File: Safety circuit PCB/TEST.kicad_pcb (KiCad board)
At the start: 2 copper layers, 101.5 x 54.2 mm, 36 parts, among them J1 430450801, J2 430450801, Q1 2N7002K, Q2 2N7002K, Q3 2N7002K, Q4 2N7002K, Q5 2N7002K, Q6 2N7002K, Q7 2N7002K

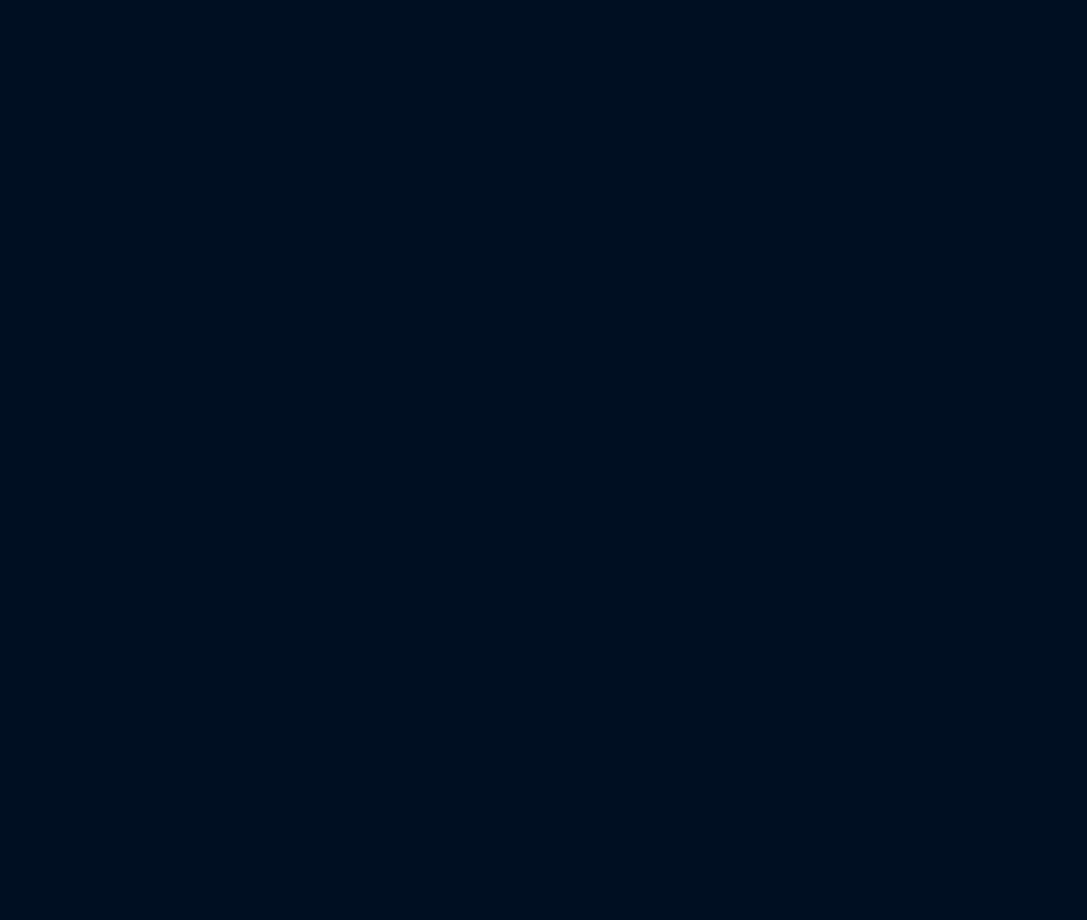
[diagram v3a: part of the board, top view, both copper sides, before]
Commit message: Add Sammy connector footprint to Safety Circuit PCB
The PCB layout still needs to be redone once again to actually fit the connector. It seems like it will have to be extended around 0.8 inches. at a minimum.
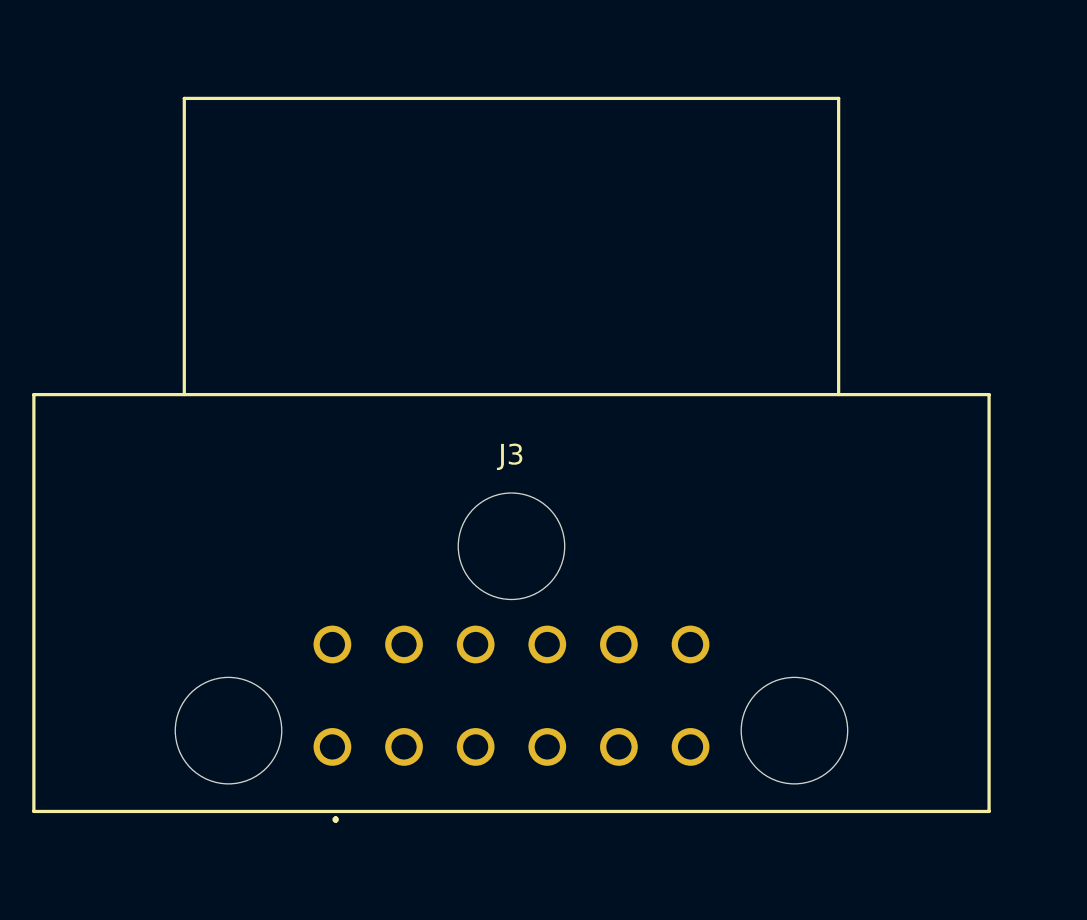
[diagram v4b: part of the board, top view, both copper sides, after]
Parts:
- added J3: DT13-12PA-B016, SC:DT1312PAB016, F.Cu at (38.2, 93.4)

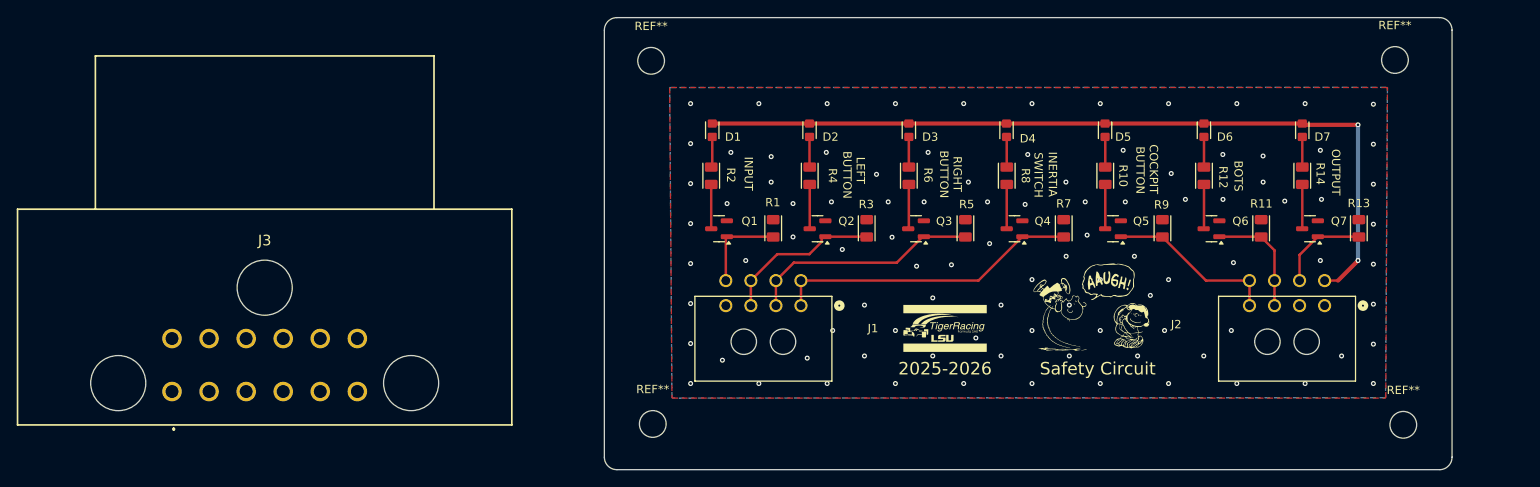
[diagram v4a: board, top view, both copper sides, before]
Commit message: Safety Circuit - Add Sammy Connector, Generate BOM, Generate Gerber and Drill Files
Safety circuit is about half an inch wider and half and inch less tall now
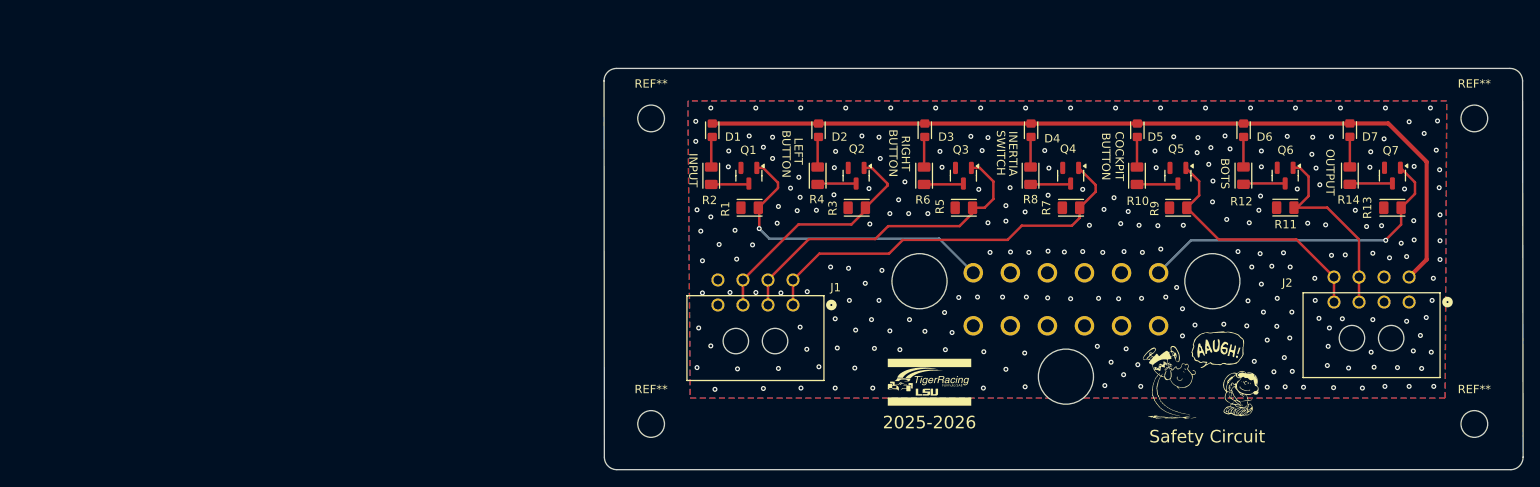
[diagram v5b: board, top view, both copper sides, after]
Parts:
- J3: moved to B.Cu
- moved J3 97.0 mm to (134.2, 79.2)
- moved Safety Circuit 15.4 mm to (161.4, 91.5)
- moved REF** 11.8 mm to (194.2, 60.7)
- moved Q7 11.7 mm to (184.4, 67.5), turned to -90 degrees
- moved Q6 10.9 mm to (171.6, 67.5), turned to -90 degrees
- moved J2 10.1 mm to (186.4, 82.7)
- moved Q5 10.0 mm to (158.7, 67.6), turned to -90 degrees
- moved Q4 9.25 mm to (145.9, 67.6), turned to -90 degrees
- moved Q3 8.52 mm to (133.0, 67.6), turned to -90 degrees
- moved REF** 8.51 mm to (194.2, 97.3)
- moved Q2 7.86 mm to (120.2, 67.6), turned to -90 degrees
- moved Q1 7.29 mm to (107.3, 67.6), turned to -90 degrees
- moved REF** 6.90 mm to (95.6, 60.7)
- moved 2025-2026 6.71 mm to (128.9, 92.3)
- moved D7 5.70 mm to (179.3, 62.1)
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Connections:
- J1 pad 8: /INPUT -> unconnected-(J1-Pad8)
- J2 pad 6: /OUTPUT -> unconnected-(J2-Pad6)
- J3 pad 1: unconnected-(J3-Pad1) -> /INPUT
- J3 pad 6: unconnected-(J3-Pad6) -> /OUTPUT
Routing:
- net /OUTPUT: track 11.0 -> 39.7 mm, vias 0 -> 1
- net /INPUT: track 10.6 -> 37.5 mm, vias 0 -> 1
- net /RIGHT_BUTTON: track 27.6 -> 39.8 mm
- net /INERTIA_SWITCH: track 36.5 -> 48.0 mm
- net /LEFT_BUTTON: track 18.8 -> 28.7 mm
- net /BOTS: track 13.7 -> 23.5 mm
- net /COCKPIT_BUTTON: track 20.4 -> 30.1 mm
- net +12V: track 98.7 -> 102.1 mm, vias 2 -> 0
- net Net-(Q1-D): track 5.31 -> 4.41 mm
- net Net-(Q2-D): track 5.31 -> 4.51 mm
- net Net-(Q3-D): track 5.35 -> 4.61 mm
- net Net-(Q4-D): track 5.31 -> 4.71 mm
- net Net-(Q5-D): track 5.32 -> 4.80 mm
- net GND: vias 98 -> 248
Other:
- board size 101.5 x 54.2 mm -> 110.1 x 48.1 mm

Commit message: Connector refactor
Add nanofit for input and output, remove two 8-pin connectors. Still need to stitch board and regenerate gerbers.
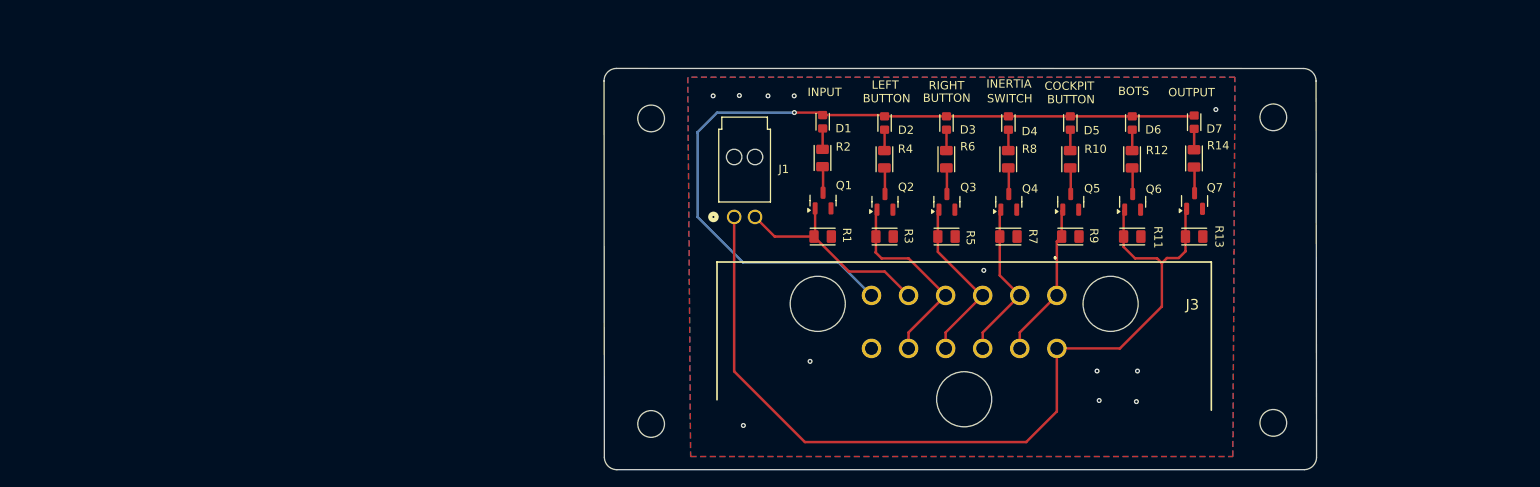
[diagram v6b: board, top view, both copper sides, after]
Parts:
- removed 2025-2026: LOGO, SC:tiger-racing-logo-with-name-10mm-by-5.6mm
- removed J2: 430450801, SC:CONN_SD-43045-001_08_MOL
- removed Safety Circuit: LOGO, SC:charlie-brown-lucy-football
- J1: value 430450801 -> 1053131202; footprint SC:CONN_SD-43045-001_08_MOL -> SC:CONN_SD-105313-100_02_MOL
- J3: moved to F.Cu
- moved REF** 24.1 mm to (170.1, 97.2)
- moved REF** 24.1 mm to (170.1, 60.6)
- moved R13 24.0 mm to (160.7, 74.8), turned to 0 degrees
- moved Q7 23.9 mm to (160.7, 70.6), turned to 90 degrees
- moved R14 18.8 mm to (160.6, 65.5)
- moved D7 18.7 mm to (160.7, 61.1)
- moved R11 18.7 mm to (153.2, 74.8), turned to 0 degrees
- moved Q6 18.5 mm to (153.3, 70.7), turned to 90 degrees
- moved R2 13.5 mm to (116.1, 65.4)
- moved R12 13.5 mm to (153.2, 65.6)
- moved R9 13.4 mm to (145.8, 74.8), turned to 0 degrees
- moved D6 13.4 mm to (153.2, 61.2)
- moved D1 13.3 mm to (116.2, 61.1)
- moved Q5 13.2 mm to (145.9, 70.7), turned to 90 degrees
- moved J1 12.7 mm to (105.5, 72.5), turned to 180 degrees
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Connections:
- J1 pad 1: /INERTIA_SWITCH -> /BOTS_END
- J1 pad 2: /RIGHT_BUTTON -> /INPUT
- J3 pad 1: /INPUT -> /BOTS_START
- J3 pad 10: unconnected-(J3-Pad10) -> /COCKPIT_BUTTON_START
- J3 pad 11: unconnected-(J3-Pad11) -> /BOTS_START
- J3 pad 12: unconnected-(J3-Pad12) -> /BOTS_END
- J3 pad 2: unconnected-(J3-Pad2) -> /COCKPIT_BUTTON_START
- J3 pad 3: unconnected-(J3-Pad3) -> /INERTIA_SWITCH_START
- J3 pad 4: unconnected-(J3-Pad4) -> /LEFT_BUTTON_END
- J3 pad 5: unconnected-(J3-Pad5) -> /INPUT
- J3 pad 6: /OUTPUT -> +12V
- J3 pad 7: unconnected-(J3-Pad7) -> GND
- J3 pad 8: unconnected-(J3-Pad8) -> /LEFT_BUTTON_END
- J3 pad 9: unconnected-(J3-Pad9) -> /INERTIA_SWITCH_START
- Q2 pad 1: /LEFT_BUTTON -> /LEFT_BUTTON_END
- Q3 pad 1: /RIGHT_BUTTON -> /INERTIA_SWITCH_START
- Q4 pad 1: /INERTIA_SWITCH -> /COCKPIT_BUTTON_START
- Q5 pad 1: /COCKPIT_BUTTON -> /BOTS_START
- Q6 pad 1: /BOTS -> /BOTS_END
- Q7 pad 1: /OUTPUT -> /BOTS_END
- R11 pad 1: /BOTS -> /BOTS_END
- R13 pad 1: /OUTPUT -> /BOTS_END
- R3 pad 1: /LEFT_BUTTON -> /LEFT_BUTTON_END
- R5 pad 1: /RIGHT_BUTTON -> /INERTIA_SWITCH_START
- R7 pad 1: /INERTIA_SWITCH -> /COCKPIT_BUTTON_START
- R9 pad 1: /COCKPIT_BUTTON -> /BOTS_START
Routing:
- net /BOTS_END: track 0.00 -> 108.1 mm
- net /INERTIA_SWITCH: track 48.0 -> 0.00 mm
- net /RIGHT_BUTTON: track 39.8 -> 0.00 mm
- net /OUTPUT: track 39.7 -> 0.00 mm, vias 1 -> 0
- net /COCKPIT_BUTTON: track 30.1 -> 0.00 mm
- net /LEFT_BUTTON: track 28.7 -> 0.00 mm
- net /LEFT_BUTTON_END: track 0.00 -> 23.9 mm
- net /BOTS: track 23.5 -> 0.00 mm
- net /INERTIA_SWITCH_START: track 0.00 -> 20.8 mm
- net /COCKPIT_BUTTON_START: track 0.00 -> 19.5 mm
- net /BOTS_START: track 0.00 -> 18.8 mm
- net /INPUT: track 37.5 -> 25.7 mm, vias 1 -> 0
- net +12V: track 102.1 -> 94.8 mm, vias 0 -> 1
- net Net-(Q7-D): track 5.00 -> 3.15 mm
- net Net-(Q6-D): track 4.90 -> 3.15 mm
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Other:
- board size 110.1 x 48.1 mm -> 85.3 x 48.1 mm
- board text added: "1"
- board text added: "10"
- board text added: "11"
- board text added: "12"
- board text added: "12V"
- board text added: "2"
- board text added: "3"
- board text added: "4"
- board text added: "5"
- board text added: "6"
- board text added: "7"
- board text added: "8"
- board text added: "9"
- board text added: "BOTS_E"
- board text added: "BOTS_S"
- board text added: "CB_E"
- board text added: "CB_S"
- board text added: "GND"
- board text added: "IN"
- board text added: "IS_E"
- board text added: "IS_S"
- board text added: "LB_E"
- board text added: "LB_S"
- board text added: "OUT"
- board text added: "RB_E"
- board text added: "RB_S"
